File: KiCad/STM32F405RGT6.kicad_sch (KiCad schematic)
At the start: 51 parts, among them J1 Conn_02x05_Odd_Even, J2 USB_C_Receptacle_USB2.0, SW1 TS-1187A, SW2 TS-1187A, U1 M24C02-RMN, U2 STM32F405RGTx, U3 AMS1117-3.3, U4 SRV05-4, Y1 16MHz

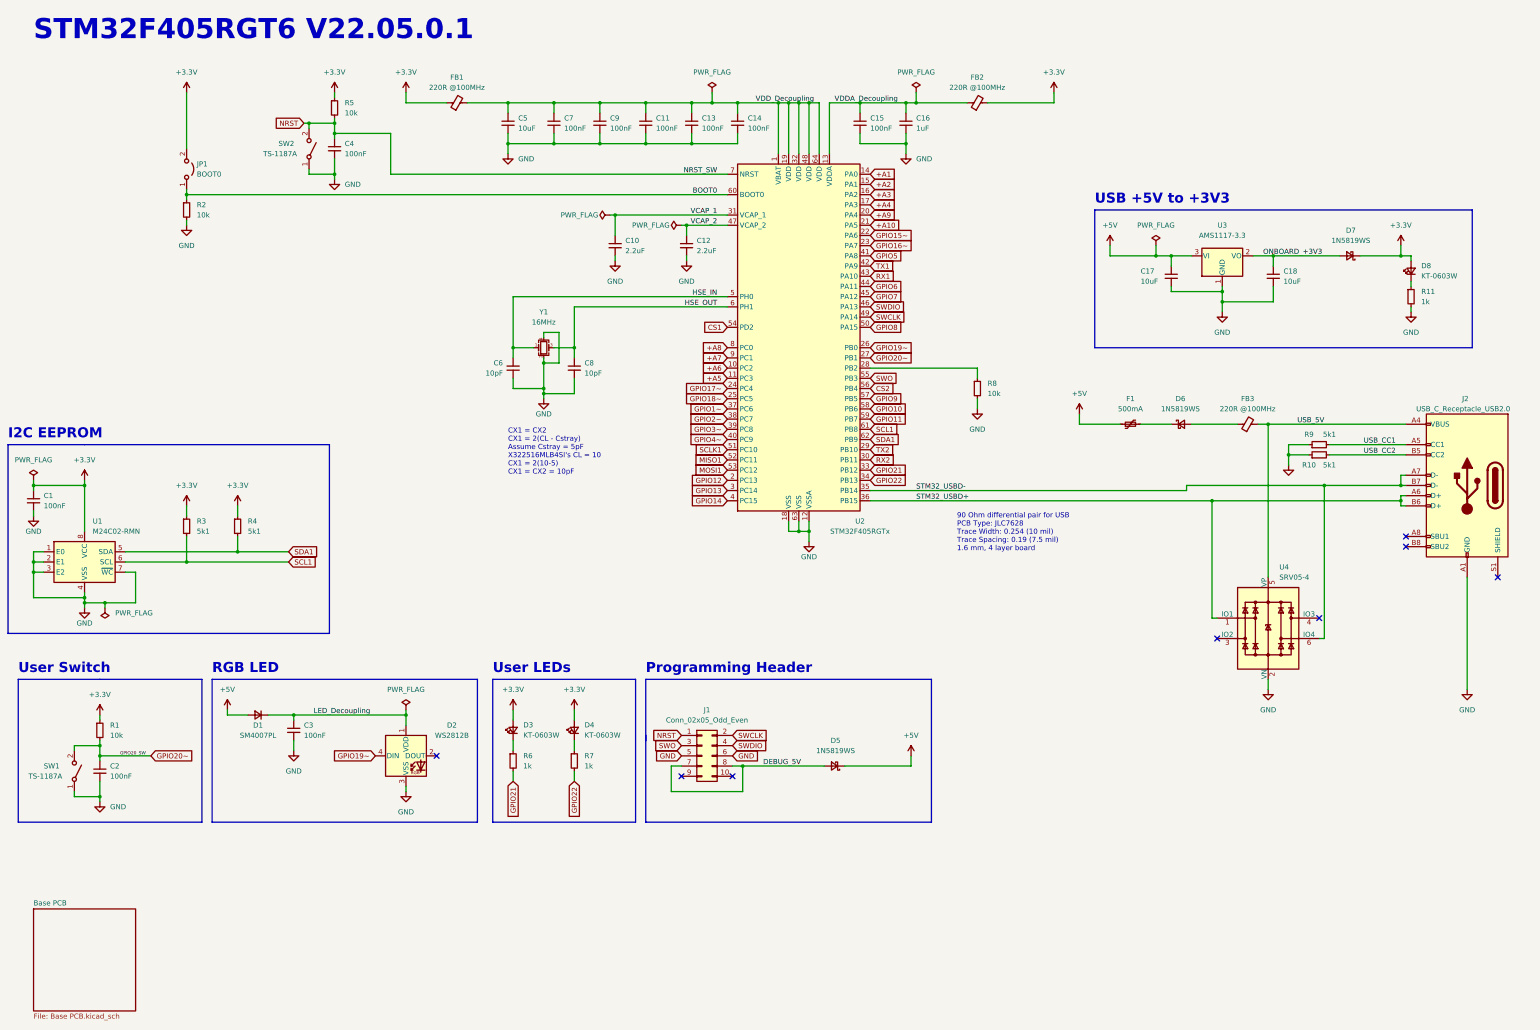
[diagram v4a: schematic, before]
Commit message: Changed Pin Mapping
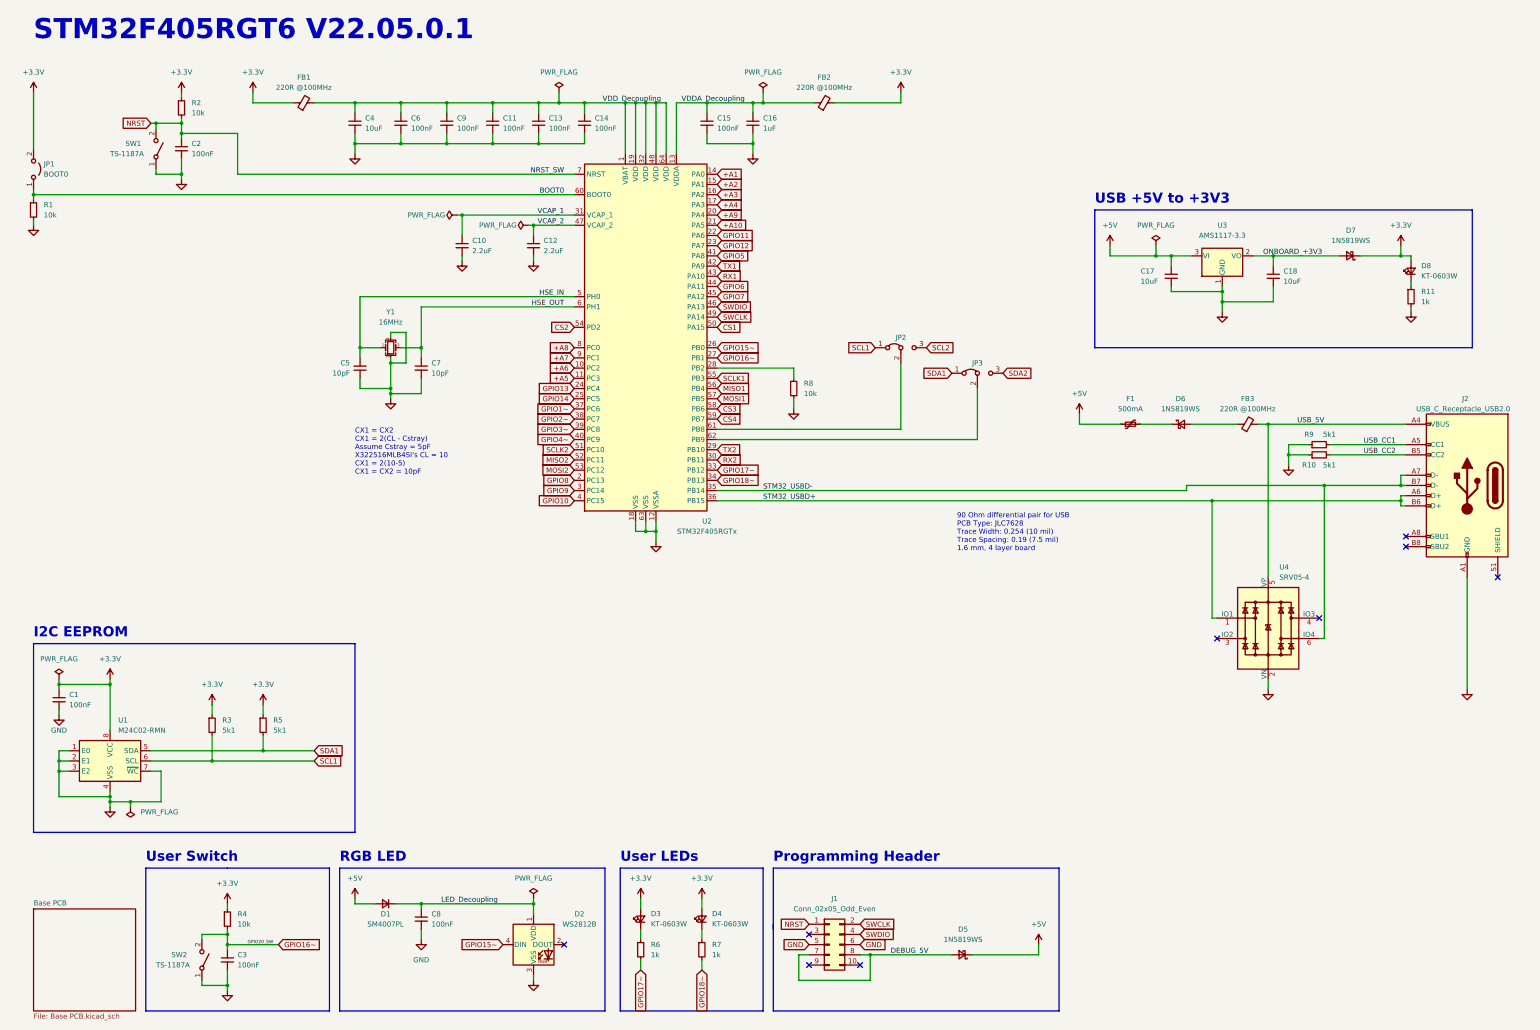
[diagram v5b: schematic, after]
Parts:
- added JP2, JP3: SDA_Jumper, Jumper:SolderJumper-3_P1.3mm_Bridged12_RoundedPad1.0x1.5mm, symbol Jumper:Jumper_3_Bridged12
- renumbered C4 to C2, C2 to C3, C5 to C4, C6 to C5, C7 to C6, C8 to C7, C3 to C8, R2 to R1, R5 to R2, R1 to R4, R4 to R5, SW2 to SW1, SW1 to SW2
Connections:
- net GPIO19~ is gone; now on net GPIO15~: D2.4 (DIN), U2.26 (PB0)
- net GPIO20~ is gone; now on net GPIO16~: C3.1, R4.2, SW2.2 (B), U2.27 (PB1)
- net GPIO21 is gone; now on net GPIO17~: R6.2, U2.33 (PB12)
- net GPIO22 is gone; now on net GPIO18~: R7.2, U2.34 (PB13)
- net CS1: now also U2.50 (PA15); no longer U2.54 (PD2)
- net CS2: now also U2.54 (PD2); no longer U2.56 (PB4)
- net GPIO10: now also U2.4 (PC15); no longer U2.58 (PB6)
- net GPIO11: now also U2.22 (PA6); no longer U2.59 (PB7)
- net GPIO12: now also U2.23 (PA7); no longer U2.2 (PC13)
- net GPIO13: now also U2.24 (PC4); no longer U2.3 (PC14)
- net GPIO14: now also U2.25 (PC5); no longer U2.4 (PC15)
- net GPIO15~: no longer U2.22 (PA6)
- net GPIO16~: no longer U2.23 (PA7)
- net GPIO17~: no longer U2.24 (PC4)
- net GPIO18~: no longer U2.25 (PC5)
- net GPIO8: now also U2.2 (PC13); no longer U2.50 (PA15)
- net GPIO9: now also U2.3 (PC14); no longer U2.57 (PB5)
- net MISO1: now also U2.56 (PB4); no longer U2.52 (PC11)
- net MOSI1: now also U2.57 (PB5); no longer U2.53 (PC12)
- net SCL1: now also JP2.1 (A); no longer U2.61 (PB8)
- net SCLK1: now also U2.55 (PB3); no longer U2.51 (PC10)
- net SDA1: now also JP3.1 (A); no longer U2.62 (PB9)
- net SWO: no longer names the net of J1.3 (Pin_3)
- net SWO: no longer U2.55 (PB3)
- new net: JP3.2 (C), U2.62 (PB9)
- new net: JP2.2 (C), U2.61 (PB8)
- new net CS3: U2.58 (PB6)
- new net CS4: U2.59 (PB7)
- new net MISO2: U2.52 (PC11)
- new net MOSI2: U2.53 (PC12)
- new net SCL2: JP2.3 (B)
- new net SCLK2: U2.51 (PC10)
- new net SDA2: JP3.3 (B)
- no-connect marks 8 -> 9
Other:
- moved on the sheet: C1, C10, C11, C12, C13, C14, C15, C16, C2, C3, C4, C5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

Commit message: Updated PCB and Schematic
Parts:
- removed JP2, JP3: SDA_Jumper, Jumper:SolderJumper-3_P1.3mm_Bridged12_RoundedPad1.0x1.5mm, symbol Jumper:Jumper_3_Bridged12
- added JP2: SCL_Jumper, Jumper:SolderJumper-2_P1.3mm_Open_RoundedPad1.0x1.5mm, symbol Jumper:Jumper_2_Open
- added JP3: SDA_Jumper, Jumper:SolderJumper-2_P1.3mm_Open_RoundedPad1.0x1.5mm, symbol Jumper:Jumper_2_Open
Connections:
- net SCL1: now also U2.61 (PB8), JP2.1 (A)
- net SCL2: now also JP2.2 (B)
- net SDA1: now also U2.62 (PB9), JP3.1 (A)
- net SDA2: now also JP3.2 (B)

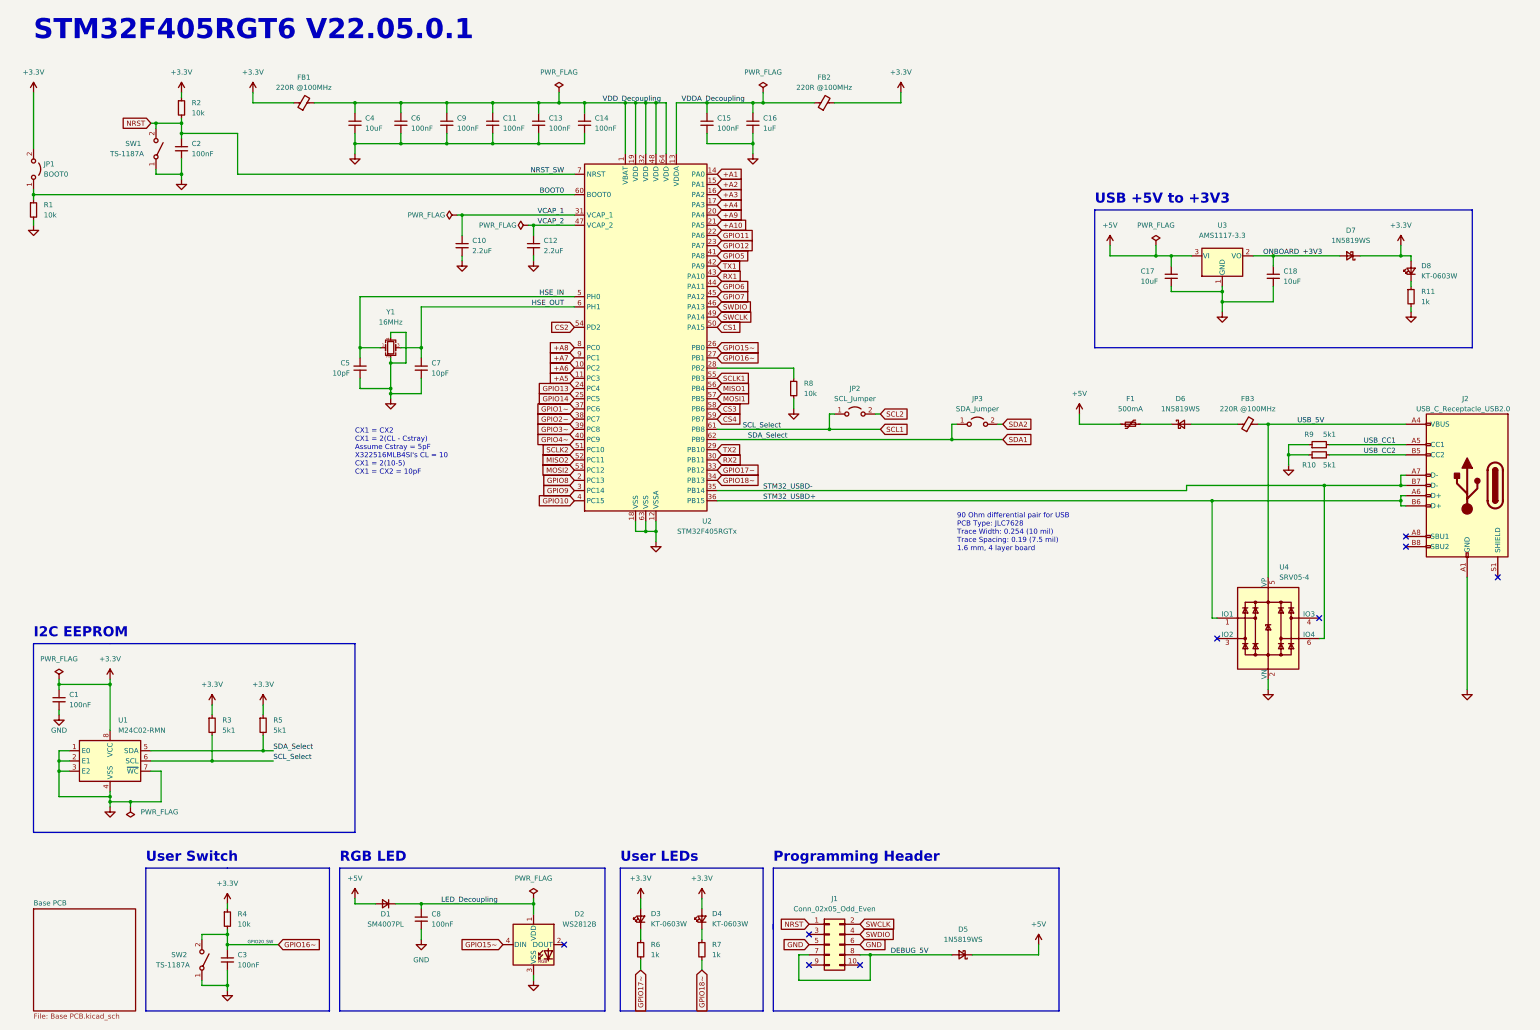
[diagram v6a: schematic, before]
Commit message: Changed some components
added a PNP mosfet onto the onboard 3.3V regulator to stop the diode drop.
changed the ESD protection on the USB to allow for more clearance
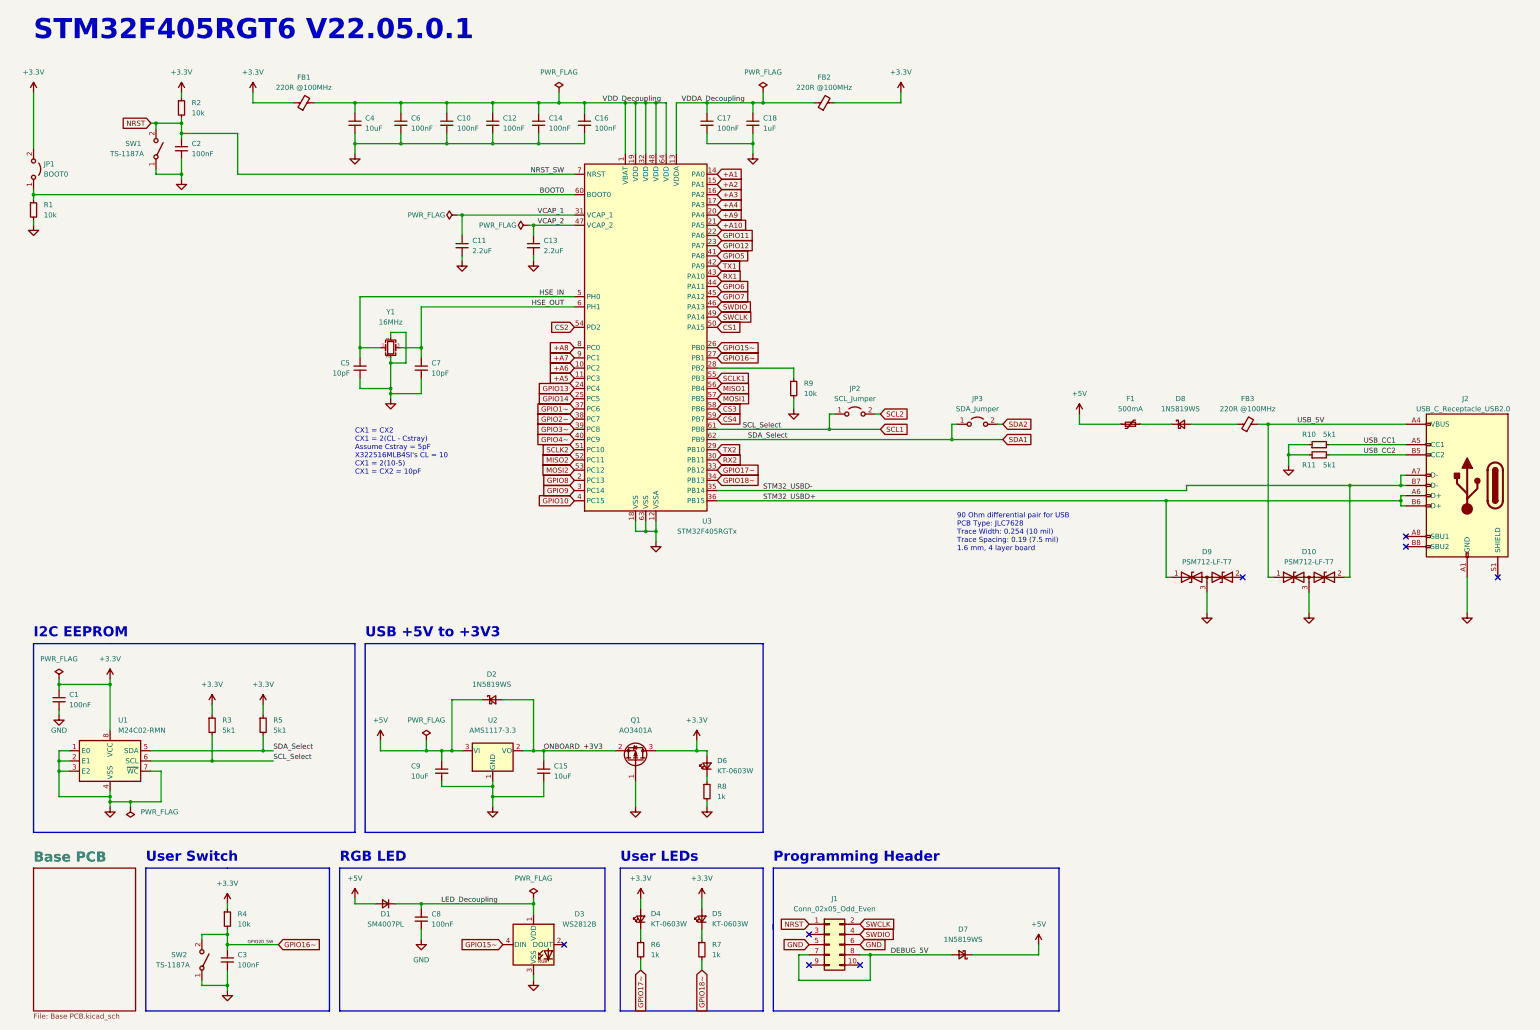
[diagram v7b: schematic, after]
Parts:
- removed D7: 1N5819WS, Diode_SMD:D_SOD-323, symbol Device:D_Schottky_Small
- removed U4: SRV05-4, Package_TO_SOT_SMD:SOT-23-6, symbol Power_Protection:SRV05-4
- added D10, D9: PSM712-LF-T7, Package_TO_SOT_SMD:SOT-23, symbol Device:D_TVS_Dual_AAC
- added D2: 1N5819WS, Diode_SMD:D_SOD-323, symbol Device:D_Schottky_Small
- added Q1: AO3401A, Package_TO_SOT_SMD:SOT-23, symbol Transistor_FET:AO3401A
- renumbered C9 to C10, C10 to C11, C11 to C12, C12 to C13, C13 to C14, C18 to C15, C14 to C16, C15 to C17, C16 to C18, C17 to C9, D2 to D3, D3 to D4, D4 to D5, D8 to D6, D5 to D7, D6 to D8, R9 to R10, R10 to R11, R11 to R8, R8 to R9, U3 to U2, U2 to U3
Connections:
- net +3V3: now also Q1.3 (D)
- net +5V: now also D2.1 (K)
- net GND: now also D10.3 (common), D9.3 (common), Q1.1 (G)
- net ONBOARD_+3V3: now also D2.2 (A), Q1.2 (S)
- net STM32_USBD+: now also D9.1 (A1)
- net STM32_USBD-: now also D10.2 (A2)
- net USB_5V: now also D10.1 (A1)
- no-connect marks 9 -> 8
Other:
- moved on the sheet: C15, C9, D6, R8, U2
